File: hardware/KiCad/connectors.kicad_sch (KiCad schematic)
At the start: 27 parts

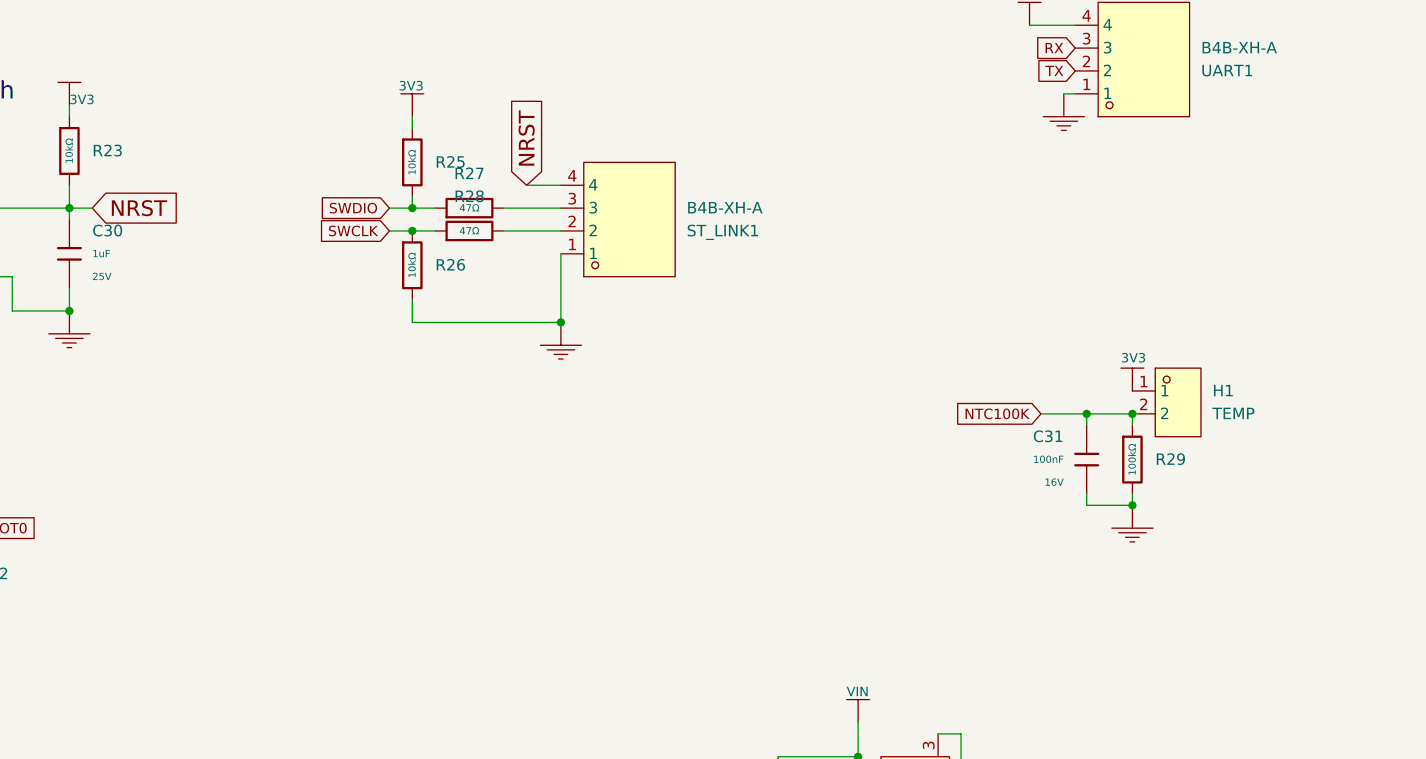
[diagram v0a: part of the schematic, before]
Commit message: Vendor easyeda2kicad component library; rename project files; fix stale part data
Vendors the 16 easyeda2kicad:* parts (symbols/footprints/3D models) that
were referenced but never committed, registers them in sym-lib-table and
a new fp-lib-table, and adds the EASYEDA2KICAD project text variable so
existing 3D-model paths resolve.

Also corrects BSC030N08NS5's stale metadata (was pointing at an ElecSuper
clone, C49108769, instead of the genuine Infineon part, C501507) and
swaps its footprint to the freshly-fetched one, and fixes STANDARDS.md's
Hardware Universe table (stale reference designators, stale MOSFET/
CC6937 LCSC numbers, ~13 previously undocumented parts, wrong library
path).

Renames the auto-generated project/sheet filenames to something legible:
ProPrj_STM32 MPPT_2024-07-25_15-40-35_2026-05-30.* -> openMPPT_v1.3.*,
and the numbered "N_Name Stuff.kicad_sch" sheets -> mcu/buck_boost/
connectors.kicad_sch. Verified via kicad-cli ERC/DRC before and after -
same violation counts, no structural breakage.

Co-Authored-By: Claude Sonnet 5 <noreply@anthropic.com>
Claude-Session: https://claude.ai/code/session_01FKwww6crXDCSrRUFRETJEs
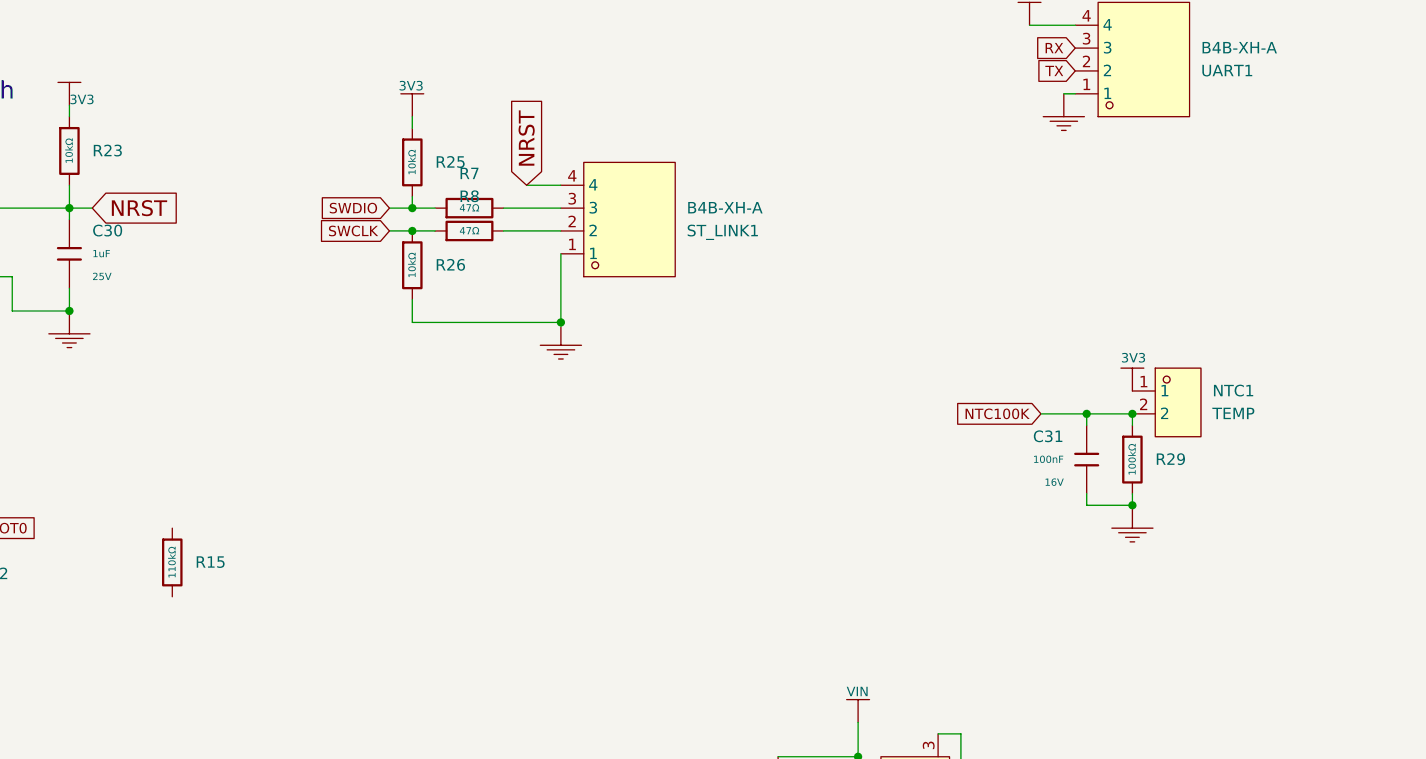
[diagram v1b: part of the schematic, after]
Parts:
- removed R27, R28: 47Ω, PCM_JLCPCB:R_0402, symbol JLCPCB-Resistors:0402,47Ω
- added R15: 110kΩ, PCM_JLCPCB:R_0603, symbol JLCPCB-Resistors:0603,110kΩ
- added R7, R8: 47Ω, PCM_JLCPCB:R_0603, symbol JLCPCB-Resistors:0603,47Ω
- GPIO1, H2, SPI/I2C1, ST_LINK1, UART1: now left out of the parts list
- NTC1: renamed from H1; now left out of the parts list
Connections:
- net SWCLK: now also R8.1
- net SWDIO: now also R7.1
- net at ST_LINK1.2: now also R8.2
- net at ST_LINK1.3: now also R7.2
